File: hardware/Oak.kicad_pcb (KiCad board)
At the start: 2 copper layers, 47 parts, among them J1 18650 Battery holder, J2 USB_B_Micro, J3 Conn_Coaxial, J4 Conn_ARM_JTAG_SWD_10, J5 Conn_01x12_Male, J6 Conn_01x12_Male, SW1 SW_SPDT, SW2 SW_Push, U1 AP2112, U2 ATSAMD21, U3 MCP7383, U4 PA1010D, U5 RFM95, U6 Waveshare_1in54_epaper

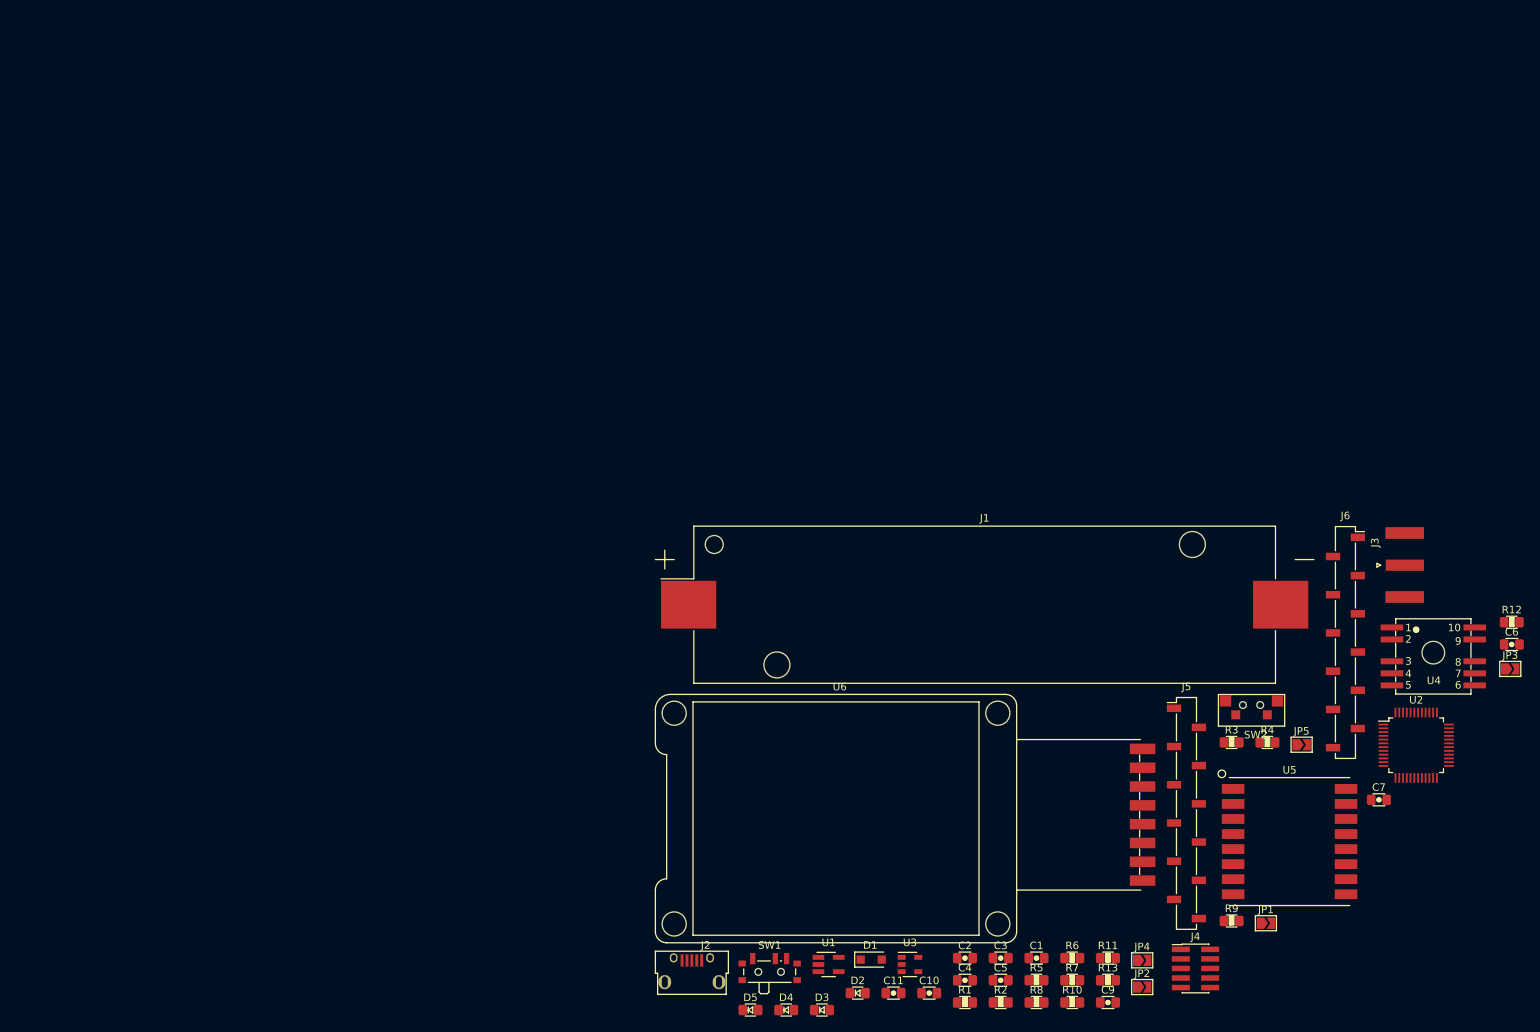
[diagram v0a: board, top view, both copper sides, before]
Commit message: feat: move logical block power components into a seperate block
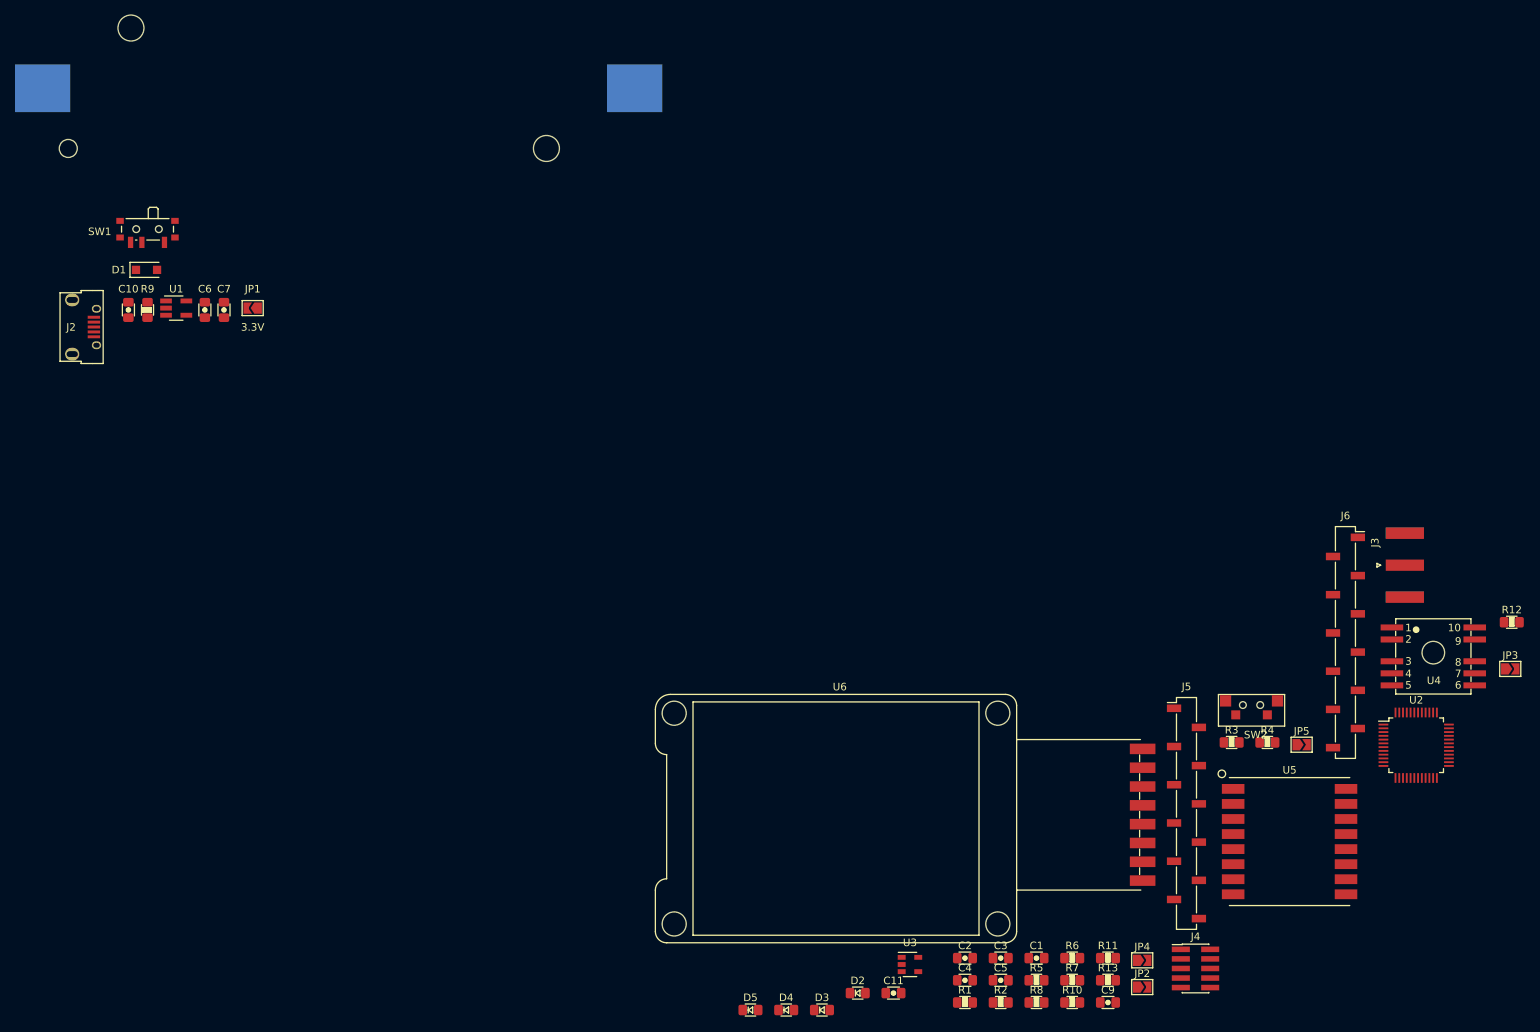
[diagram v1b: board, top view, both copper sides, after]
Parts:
- J1: moved to B.Cu
- moved C6 179.2 mm to (39.4, 56.1), turned to 270 degrees
- moved C7 166.7 mm to (41.9, 56.1), turned to 270 degrees
- moved R9 165.3 mm to (31.8, 56.1), turned to 90 degrees
- moved JP1 157.5 mm to (45.7, 55.9), turned to 180 degrees
- moved C10 139.9 mm to (29.2, 56.1), turned to 270 degrees
- moved D1 132.9 mm to (31.6, 50.8)
- moved SW1 128.2 mm to (31.8, 45.7), turned to 180 degrees
- moved U1 123.0 mm to (35.6, 55.9)
- moved J2 118.2 mm to (22.9, 58.4), turned to 270 degrees
- moved J1 109.9 mm to (57.1, 26.7)
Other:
- board text added: "3 decaps: C10, C6, C7 4 Traces out: VBUS, VBATT, USB D+/D-"
- board text added: "3.3V"

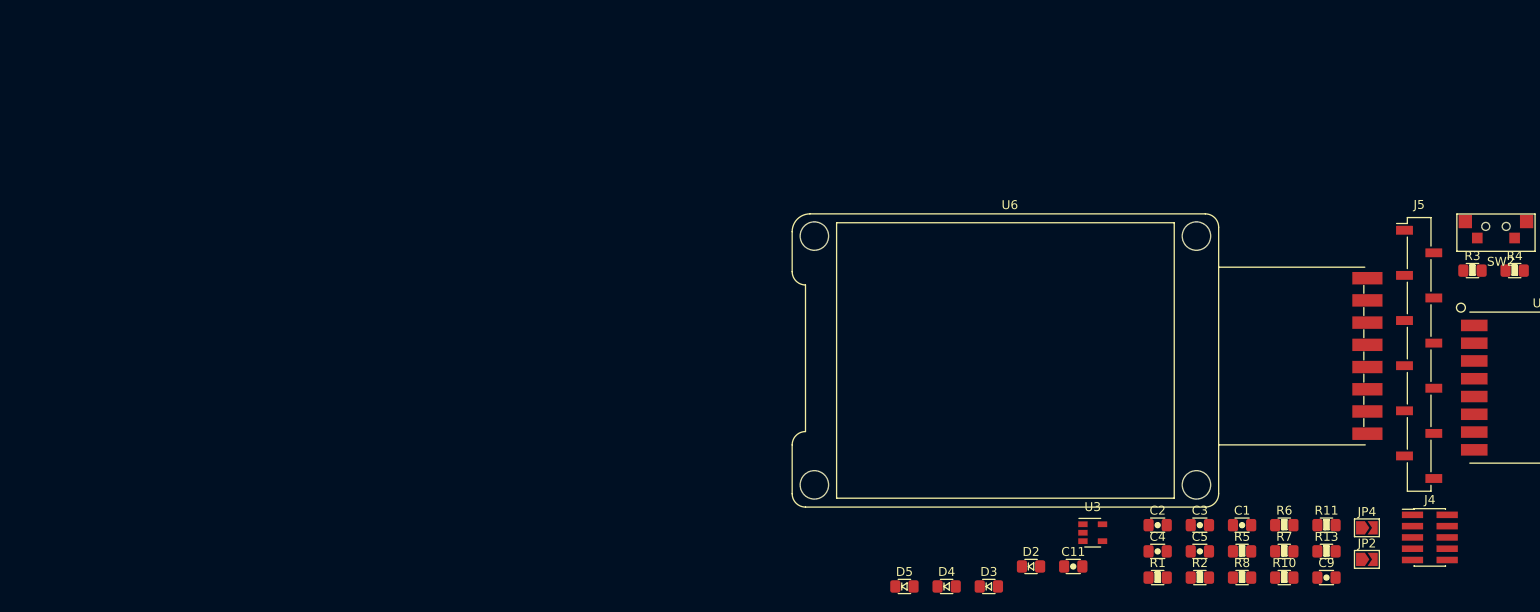
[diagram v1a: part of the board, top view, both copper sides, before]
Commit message: feat: move logical block lipo charging components into a seperate block
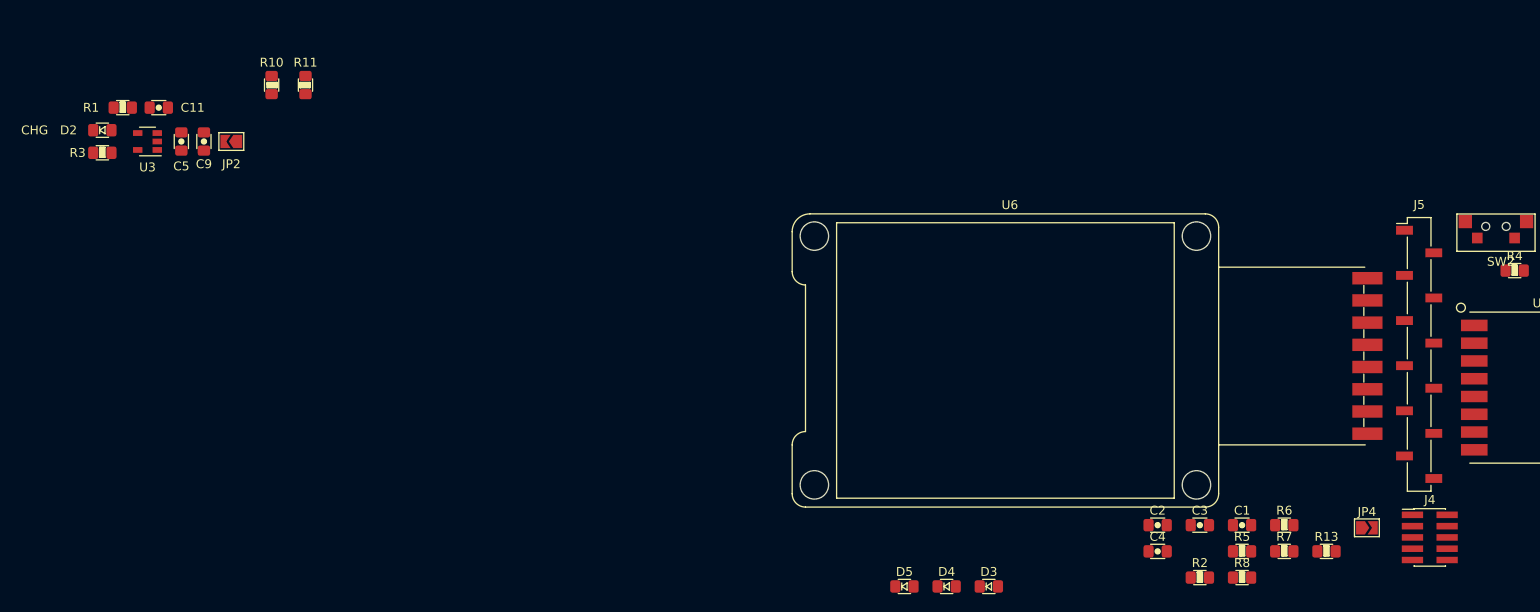
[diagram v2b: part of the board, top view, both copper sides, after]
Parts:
- moved R3 154.8 mm to (21.6, 100.3)
- moved JP2 136.2 mm to (36.1, 99.1), turned to 180 degrees
- moved C9 135.5 mm to (33.0, 99.1), turned to 90 degrees
- moved R1 127.9 mm to (23.9, 95.2)
- moved R10 126.7 mm to (40.6, 92.7), turned to 270 degrees
- moved R11 125.1 mm to (44.5, 92.7), turned to 90 degrees
- moved C5 123.6 mm to (30.5, 99.1), turned to 90 degrees
- moved D2 115.5 mm to (21.6, 97.8)
- moved C11 115.1 mm to (27.9, 95.2), turned to 180 degrees
- moved U3 115.1 mm to (26.7, 99.1), turned to 180 degrees
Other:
- board text added: "3 decaps: C10, C6, C7 4 Traces out: VBUS, VBATT, USB D+/D- 2 connectors: uUSB, Switch"
- board text added: "3 decaps: C11, C5, C9 2 Traces out: VBUS, VBAT 1 LED"
- board text added: "CHG"
- board text removed: "3 decaps: C10, C6, C7 4 Traces out: VBUS, VBATT, USB D+/D-"

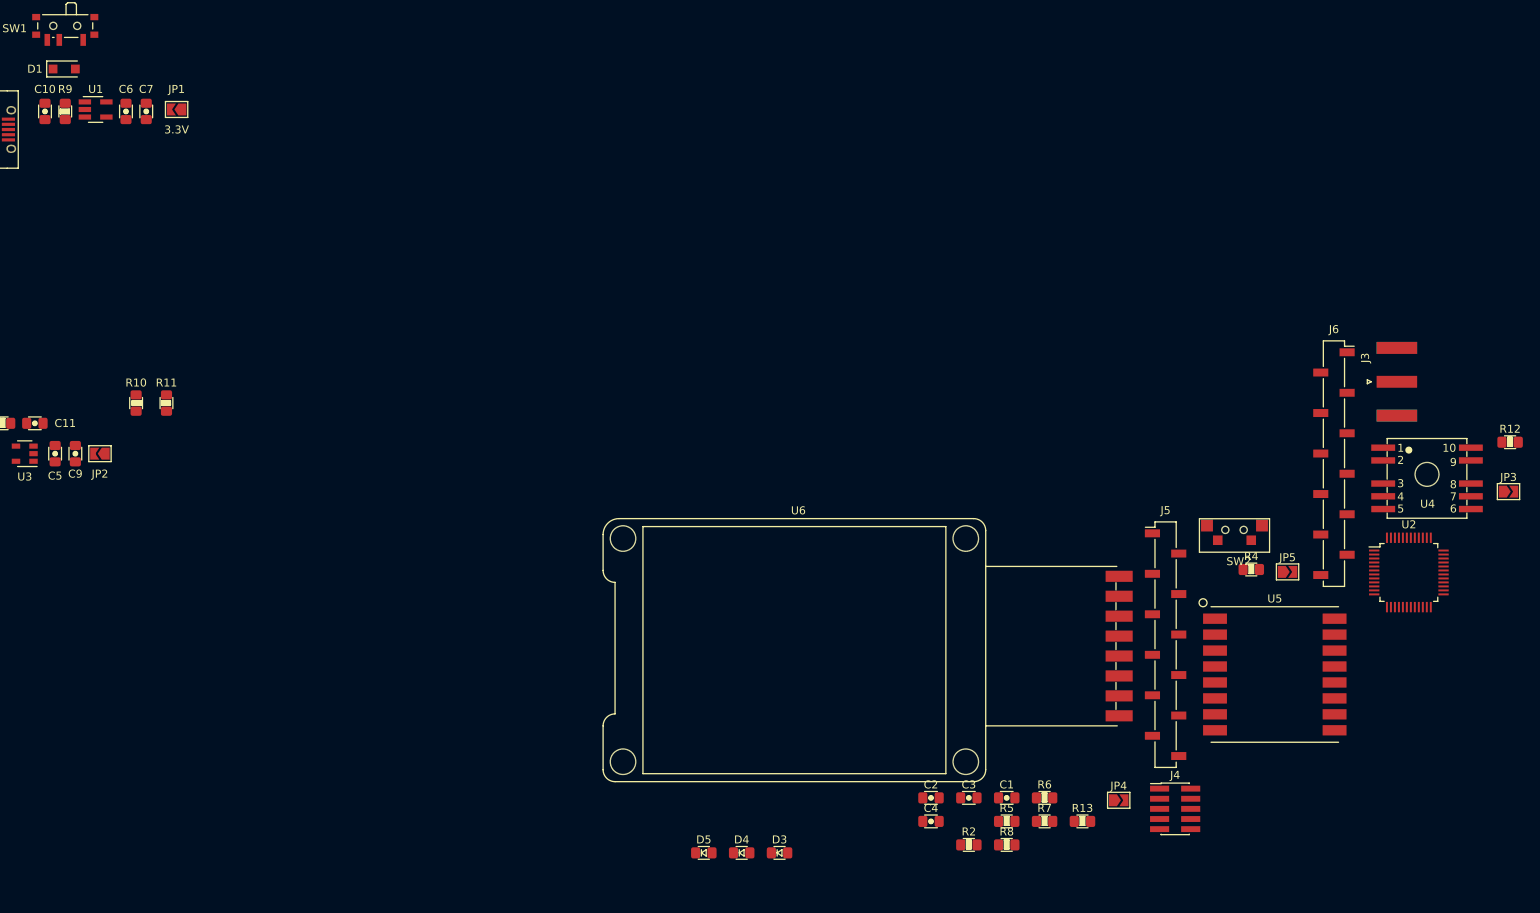
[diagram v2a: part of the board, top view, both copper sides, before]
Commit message: feat: move logical block gps components into a seperate block
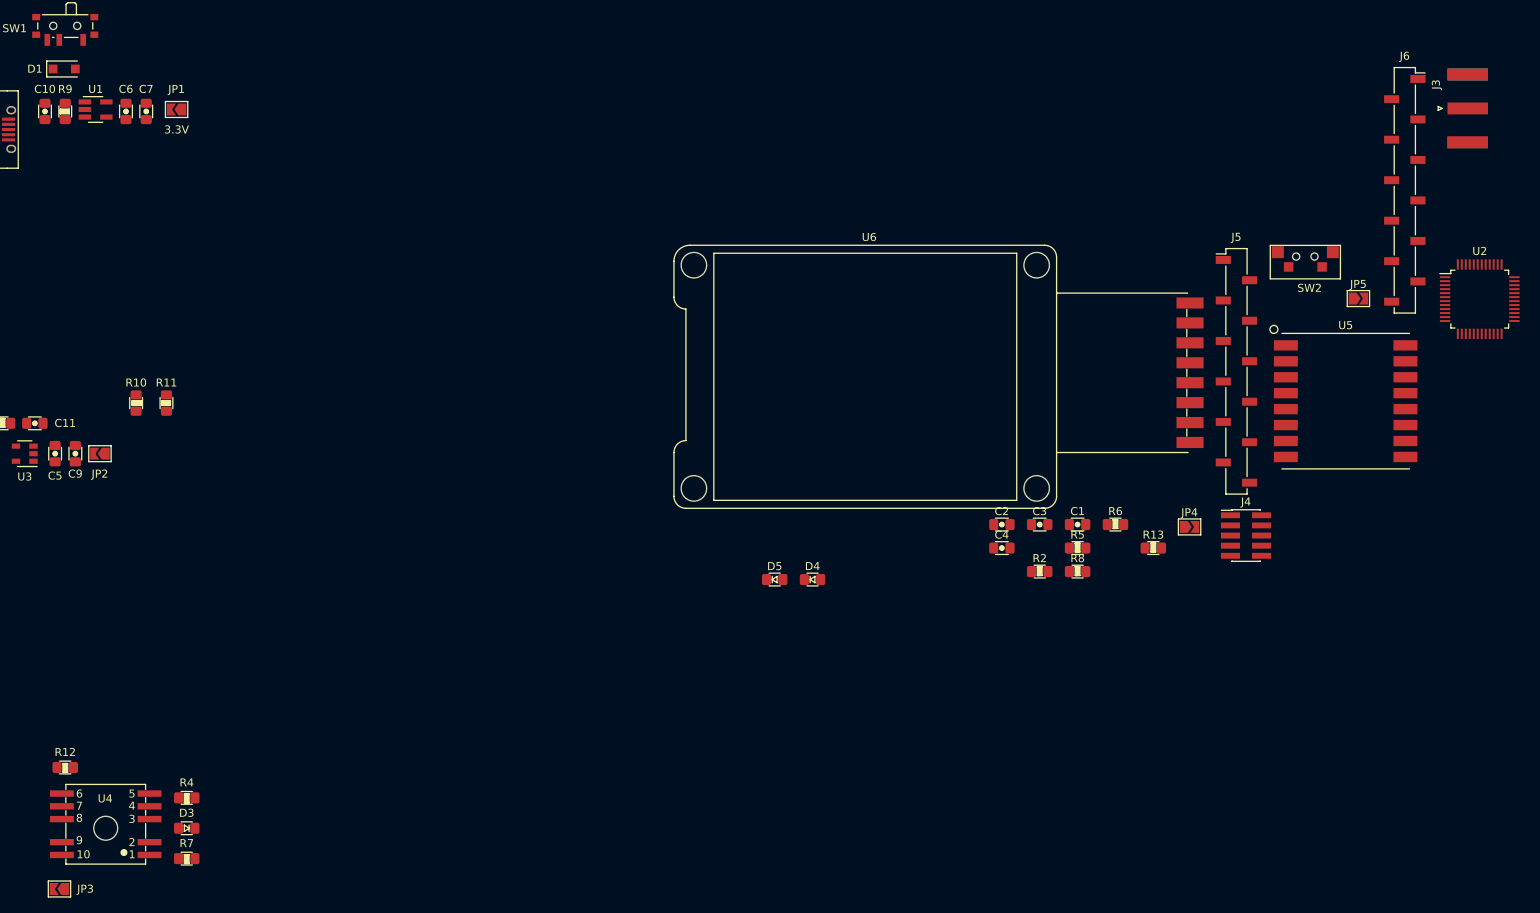
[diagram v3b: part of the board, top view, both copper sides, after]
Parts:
- moved JP3 188.5 mm to (31.0, 153.7), turned to 180 degrees
- moved R12 185.8 mm to (31.8, 138.4), turned to 180 degrees
- moved U4 171.6 mm to (36.8, 146.1), turned to 180 degrees
- moved R4 136.6 mm to (47.0, 142.2), turned to 180 degrees
- moved R7 107.7 mm to (47.0, 149.9), turned to 180 degrees
- moved D3 74.4 mm to (47.0, 146.1), turned to 180 degrees
- moved J6 35.4 mm to (199.8, 66.0)
- moved C1 35.4 mm to (158.8, 108.0)
- moved C2 35.4 mm to (149.2, 108.0)
- moved C3 35.4 mm to (154.0, 108.0)
- moved J3 35.4 mm to (207.7, 55.8)
- moved J4 35.4 mm to (179.9, 109.3)
- moved J5 35.4 mm to (178.7, 88.7)
- moved JP4 35.4 mm to (172.8, 108.2)
- moved JP5 35.4 mm to (194.0, 79.6)
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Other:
- board text added: "2 Traces out: GPS_DATA, GPS_RST 1 LED: D3"

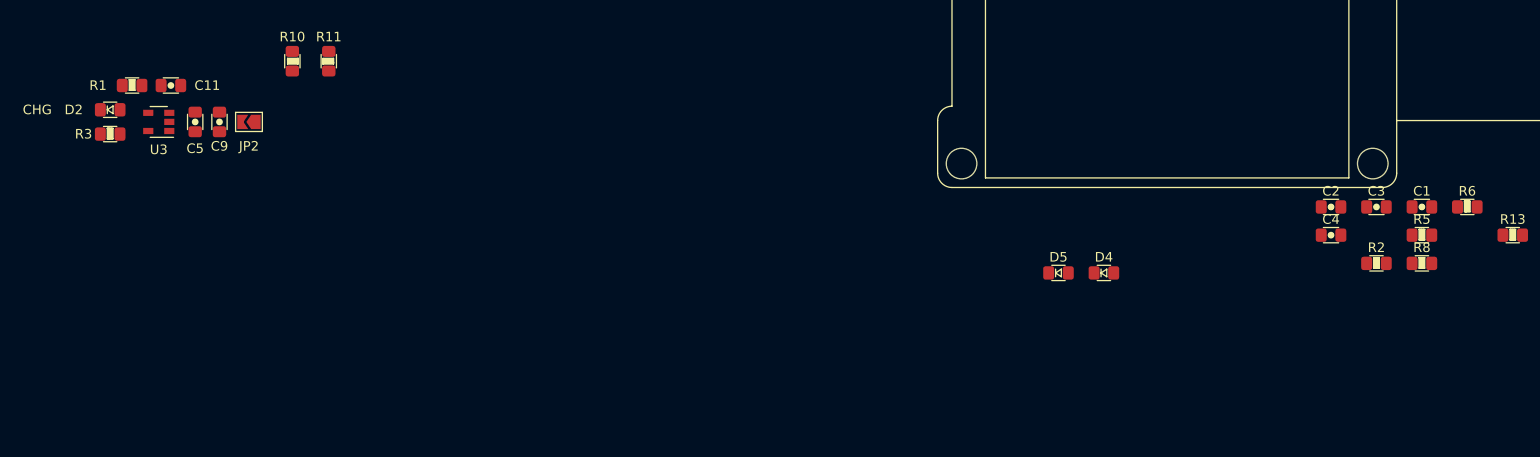
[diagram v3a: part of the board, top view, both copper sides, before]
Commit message: feat: move logical block led components into a seperate block
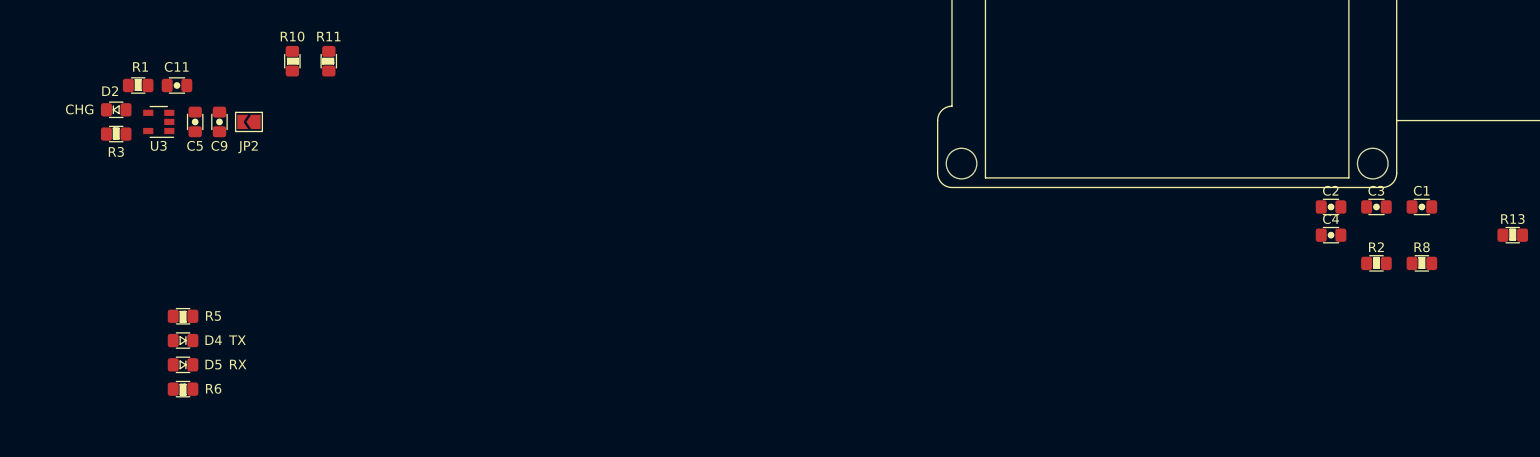
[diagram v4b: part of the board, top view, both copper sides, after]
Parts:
- moved R6 135.6 mm to (29.2, 127.0), turned to 180 degrees
- moved R5 129.8 mm to (29.2, 119.4), turned to 180 degrees
- moved D4 96.5 mm to (29.2, 121.9), turned to 180 degrees
- moved D5 92.0 mm to (29.2, 124.5), turned to 180 degrees
- moved D2 0.64 mm to (22.2, 97.8)
- moved R3 0.64 mm to (22.2, 100.3)
- moved C11 0.63 mm to (28.6, 95.2)
- moved R1 0.63 mm to (24.5, 95.2)
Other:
- board text added: "RX"
- board text added: "TX"
